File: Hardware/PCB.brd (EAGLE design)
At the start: 170.3 x 111.2 mm, 103 parts, among them IC1 BD5229G-TR, IC4 XC6220A331MR-G, J1 FH34SRJ-24S-0.5SH_99_, J2 SAMACSYS_PARTS_USB4110-GF-A, J3 QWIIC_RIGHT_ANGLE, J4 112A-TAAR-R03_ATTEND, Q1 20V/4.2A/52mΩ/1.4W, Q2 20V/4.2A/52mΩ/1.4W, Q3 SI1308EDL-T1-GE3, U1 W25Q512JVEIQ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

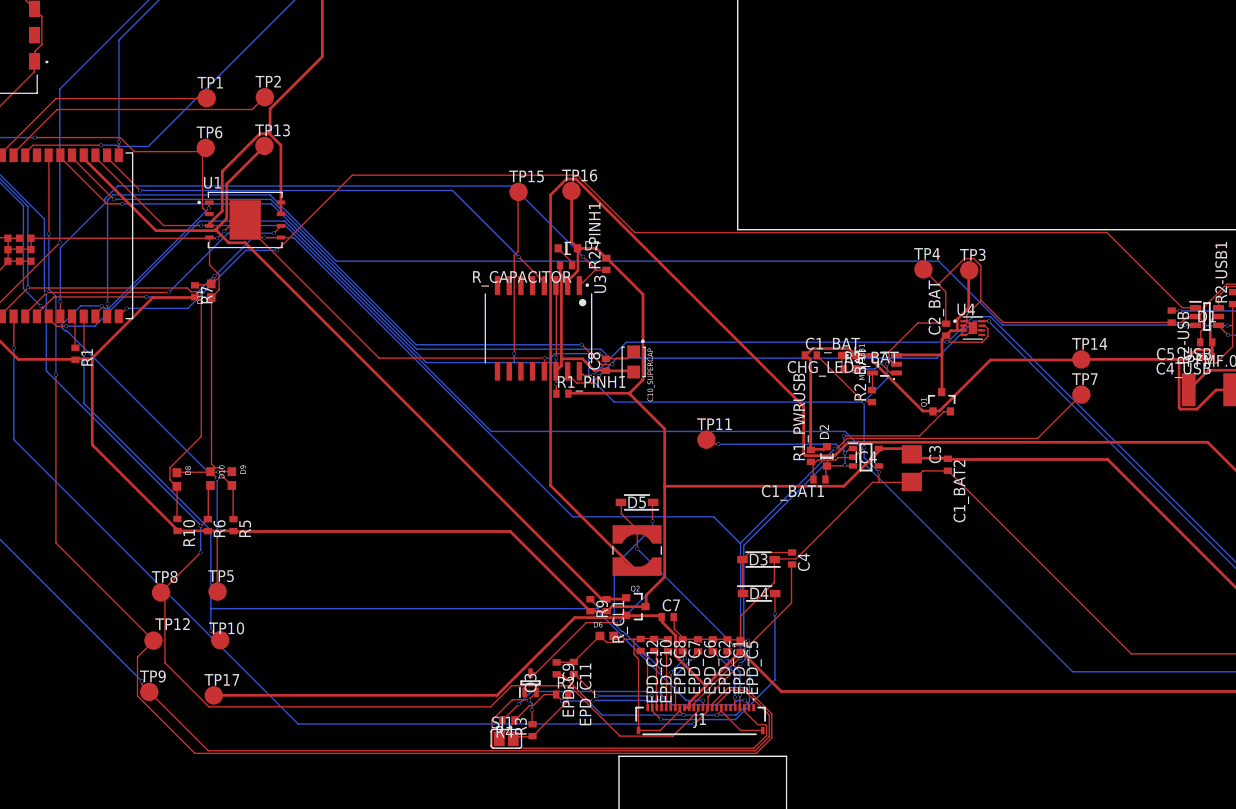
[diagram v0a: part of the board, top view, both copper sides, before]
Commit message: Added more text clarifications to PCB
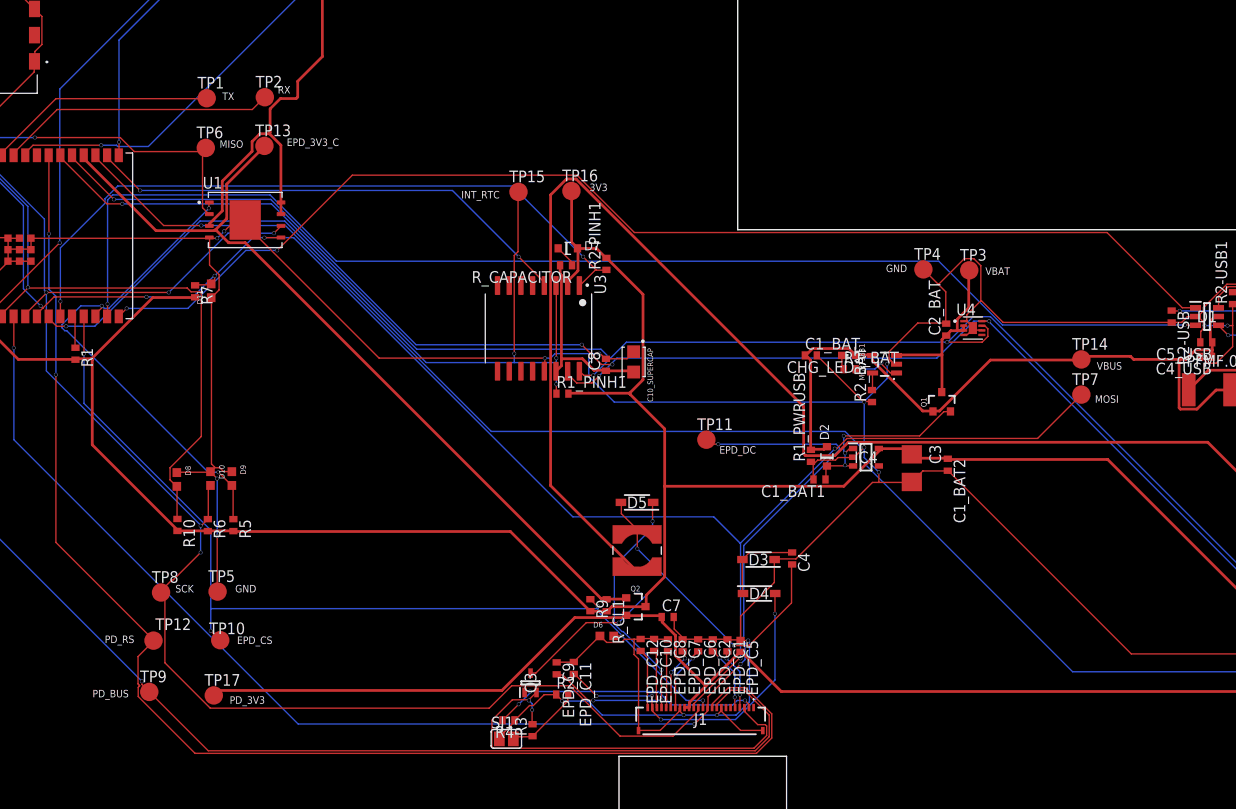
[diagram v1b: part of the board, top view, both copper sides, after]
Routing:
- net 3V3: track 427.8 -> 428.8 mm
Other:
- board text added: "3V3"
- board text added: "EPD_3V3_C"
- board text added: "EPD_CS"
- board text added: "EPD_DC"
- board text added: "GND"
- board text added: "INT_RTC"
- board text added: "MISO"
- board text added: "MOSI"
- board text added: "PD_3V3"
- board text added: "PD_BUS"
- board text added: "PD_RS"
- board text added: "RX"
- board text added: "SCK"
- board text added: "TX"
- board text added: "VBAT"
- board text added: "VBUS"

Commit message: Resolved the raised issues
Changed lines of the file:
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@@
 </via>
 <polygon width="0.1524" layer="1" spacing="1.27" pour="solid" thermals="yes">
-<vertex x="213.71515625" y="-11.6238"/>
-<vertex x="213.7431625" y="-11.6354"/>
-<vertex x="214.3238" y="-12.2160375"/>
-<vertex x="214.3238" y="137.5684375"/>
-<vertex x="213.6684375" y="138.2238"/>
-<vertex x="-18.4684375" y="138.2238"/>
-<vertex x="-19.4238" y="137.2684375"/>
-<vertex x="-19.4238" y="-11.3684375"/>
-<vertex x="-19.1684375" y="-11.6238"/>
+<vertex x="-8.4684375" y="-20.6238"/>
+<vertex x="214.0684375" y="-20.6238"/>
+<vertex x="214.5238" y="-20.1684375"/>
+<vertex x="214.5238" y="136.0238"/>
+<vertex x="-10.8238" y="136.0238"/>
+<vertex x="-10.8238" y="-18.2684375"/>
 </polygon>
 <polygon width="0.1524" layer="16" spacing="1.27" pour="solid" thermals="yes">
-<vertex x="213.51515625" y="-10.7238"/>
-<vertex x="213.5431625" y="-10.7354"/>
-<vertex x="214.3238" y="-11.5160375"/>
-<vertex x="214.3238" y="136.2684375"/>
-<vertex x="212.3684375" y="138.2238"/>
-<vertex x="-19.0684375" y="138.2238"/>
-<vertex x="-19.439321875" y="137.852915625"/>
-<vertex x="-19.442153125" y="137.848134375"/>
-<vertex x="-19.44995" y="137.8422875"/>
-<vertex x="-19.4568375" y="137.8354"/>
-<vertex x="-19.46196875" y="137.833275"/>
-<vertex x="-19.46640625" y="137.829946875"/>
-<vertex x="-19.4758375" y="137.82753125"/>
-<vertex x="-19.48484375" y="137.8238"/>
-<vertex x="-19.49039375" y="137.8238"/>
-<vertex x="-19.495771875" y="137.822421875"/>
-<vertex x="-19.50541875" y="137.8238"/>
-<vertex x="-19.51515625" y="137.8238"/>
-<vertex x="-19.520284375" y="137.825925"/>
-<vertex x="-19.52578125" y="137.826709375"/>
-<vertex x="-19.534165625" y="137.831675"/>
-<vertex x="-19.5431625" y="137.8354"/>
-<vertex x="-19.547084375" y="137.839321875"/>
-<vertex x="-19.551865625" y="137.842153125"/>
-<vertex x="-19.557715625" y="137.849953125"/>
-<vertex x="-19.5646" y="137.8568375"/>
-<vertex x="-19.566721875" y="137.8619625"/>
-<vertex x="-19.7238" y="138.0714"/>
-<vertex x="-19.7238" y="-10.7238"/>
+<vertex x="-11.4684375" y="-23.0238"/>
+<vertex x="214.8684375" y="-23.0238"/>
+<vertex x="216.6238" y="-21.2684375"/>
+<vertex x="216.6238" y="136.5238"/>
+<vertex x="-12.1684375" y="136.5238"/>
+<vertex x="-12.5238" y="136.1684375"/>
+<vertex x="-12.5238" y="-21.9684375"/>
 </polygon>
 </signal>
